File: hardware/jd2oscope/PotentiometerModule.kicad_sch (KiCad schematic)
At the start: 1 part

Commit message: feat: lot of progress
added decoupling caps, implemented a lot more of the comm. protocol stuffs, updated BNC connector to updated version, added more notes for GPIO pin I/O for future code implementation, lot of other stuff too (frankly can't remember all of it lol); I commit here b/c want to back up progress b/4 I go get smth to eat ;)
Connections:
- net reg.3.3V: now reaches VR1.1
- net POT_WIPER: now reaches VR1.2
- net GND: now reaches VR1.3
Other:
- note added: "Example of implementing POT_WIPER's GPIO pin to read % in code:"
- note added: "Key: input = 3.3V (b/c this is for logicV & we can't do 5V to GPIO pins (5V breaks them)); supplied from the 3.3V reg. on the MCU output = GND wiper = represents how much the pot. is currently rotated (i.e. the ratio between I & O)"

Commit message: feat: finished schematics
I think! Subject to change tho! for now though at least, I think they look clean asf hah~
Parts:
- renumbered VR1 to VR2
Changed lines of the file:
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@@
 		(dnp no)
 		(fields_autoplaced yes)
-		(property "Reference" "VR1"
+		(property "Reference" "VR2"
 			(at 142.24 86.36 0)
 			(effects
@@
 		)
 		(instances
-			(project ""
-				(path "/eb18a3da-9fbf-4329-a814-1afab785c817/dff6ec06-2d4b-4768-9220-df3b02ec1774"
+			(project "jd2oscope"
+				(path "/eb18a3da-9fbf-4329-a814-1afab785c817/415ed027-7cd2-4459-ae99-e85a85aec1e2/0b10fb84-a9af-450b-b4ba-7677bde7a4aa"
+					(reference "VR3")
+					(unit 1)
+				)
+				(path "/eb18a3da-9fbf-4329-a814-1afab785c817/415ed027-7cd2-4459-ae99-e85a85aec1e2/34809825-0d94-4631-a2d1-f31cc7a3b6ba"
+					(reference "VR2")
+					(unit 1)
+				)
+				(path "/eb18a3da-9fbf-4329-a814-1afab785c817/415ed027-7cd2-4459-ae99-e85a85aec1e2/4f25ad0e-659b-4d0d-998d-272f66fe29fb/a129be14-5636-4b2f-ac25-6f79cead8126"
+					(reference "VR4")
+					(unit 1)
+				)
+				(path "/eb18a3da-9fbf-4329-a814-1afab785c817/415ed027-7cd2-4459-ae99-e85a85aec1e2/4f25ad0e-659b-4d0d-998d-272f66fe29fb/d0d3e5b7-5e05-4d56-af40-3a75a71576b8"
 					(reference "VR1")
 					(unit 1)
 				)
+				(path "/eb18a3da-9fbf-4329-a814-1afab785c817/415ed027-7cd2-4459-ae99-e85a85aec1e2/9cf642e2-7276-4116-93a5-7485645ddebf/a129be14-5636-4b2f-ac25-6f79cead8126"
+					(reference "VR6")
+					(unit 1)
+				)
+				(path "/eb18a3da-9fbf-4329-a814-1afab785c817/415ed027-7cd2-4459-ae99-e85a85aec1e2/9cf642e2-7276-4116-93a5-7485645ddebf/d0d3e5b7-5e05-4d56-af40-3a75a71576b8"
+					(reference "VR5")
+					(unit 1)
+				)

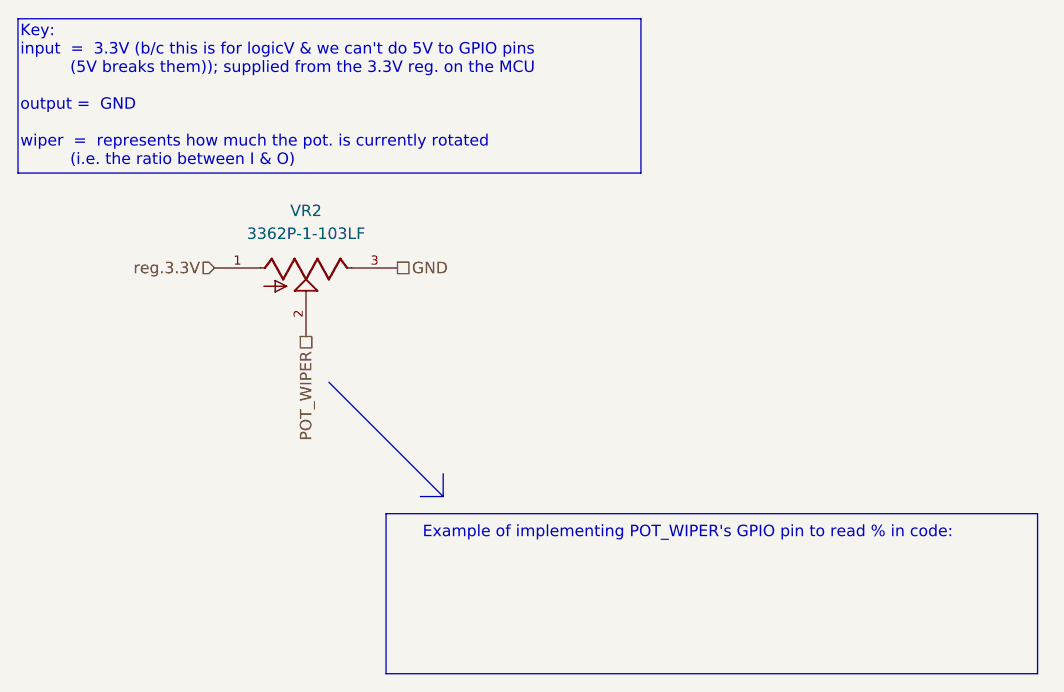
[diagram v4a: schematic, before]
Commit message: fix: added NCs
forgot to add NCs to Wroom32 dev board; they are now added!
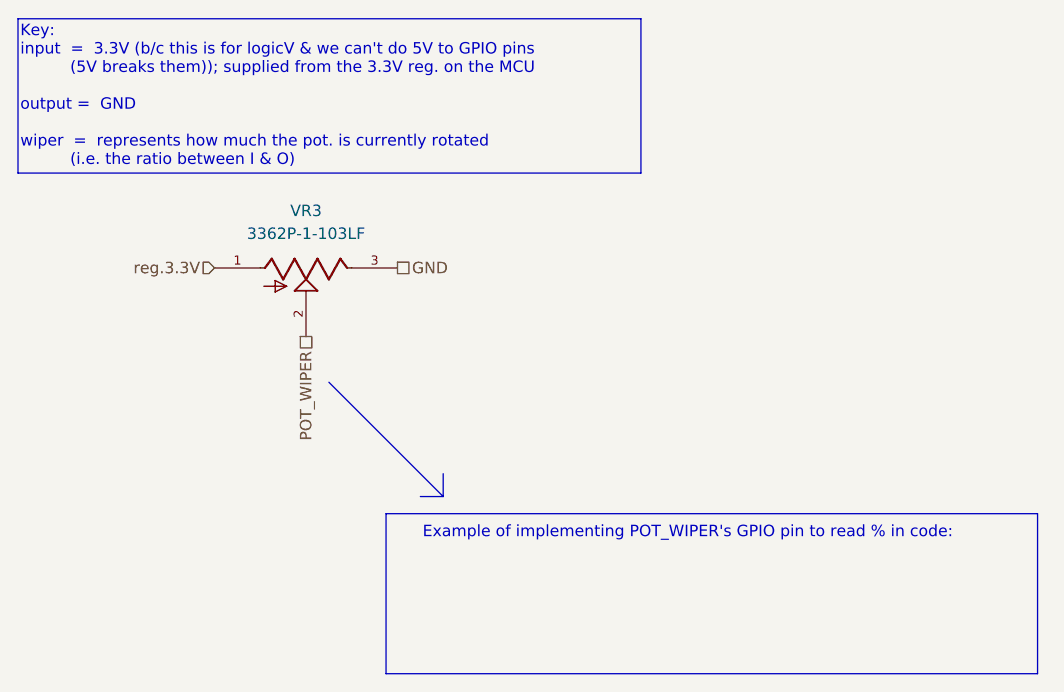
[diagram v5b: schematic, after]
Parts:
- renumbered VR2 to VR3
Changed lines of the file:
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@@
 		(dnp no)
 		(fields_autoplaced yes)
-		(property "Reference" "VR2"
+		(property "Reference" "VR3"
 			(at 142.24 86.36 0)
 			(effects

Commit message: fix: ERC funtimes
fixed a bunch of dependencies with ERC checks for the schematic; shouuuuld be easier/actually possible to open on other devices now?? (added a buncha schematics & footprints to the local files & whatnot)
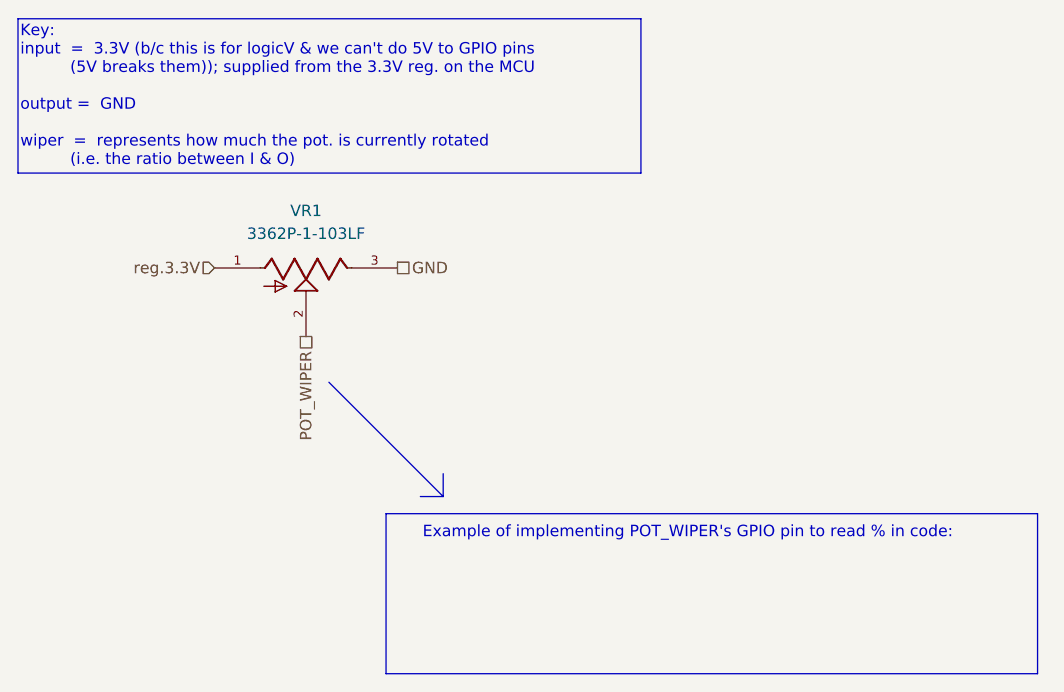
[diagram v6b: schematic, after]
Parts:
- removed VR3: 3362P-1-103LF, 3362P-1-103LF:TRIM_3362P-1-103LF, symbol pot:3362P-1-103LF
- added VR1: 3362P-1-103LF, 3362P-1-103LF:TRIM_3362P-1-103LF, symbol 3362P-1-103LF:3362P-1-103LF
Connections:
- net GND: now also VR1.3
- net POT_WIPER: now also VR1.2
- net reg.3.3V: now also VR1.1
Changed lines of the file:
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@@
 	)
 	(symbol
-		(lib_id "pot:3362P-1-103LF")
+		(lib_id "3362P-1-103LF:3362P-1-103LF")
 		(at 142.24 92.71 0)
 		(unit 1)
@@
 		(dnp no)
 		(fields_autoplaced yes)
-		(property "Reference" "VR3"
+		(property "Reference" "VR1"
 			(at 142.24 86.36 0)
 			(effects
@@
 			)
 		)
-		(property "Sim.Device" ""
-			(at 142.24 92.71 0)
-			(effects
-				(font
-					(size 1.27 1.27)
-				)
-				(hide yes)
-			)
-		)
-		(property "Sim.Params" ""
-			(at 142.24 92.71 0)
-			(effects
-				(font
-					(size 1.27 1.27)
-				)
-				(hide yes)
-			)
-		)
-		(property "Sim.Pins" ""
-			(at 142.24 92.71 0)
-			(effects
-				(font
-					(size 1.27 1.27)
-				)
-				(hide yes)
-			)
-		)
-		(property "Sim.Type" ""
-			(at 142.24 92.71 0)
-			(effects
-				(font
-					(size 1.27 1.27)
-				)
-				(hide yes)
-			)
-		)
-		(property "Comment" ""
-			(at 142.24 92.71 0)
-			(effects
-				(font
-					(size 1.27 1.27)
-				)
-				(hide yes)
-			)
-		)
-		(property "EU_RoHS_Compliance" ""
-			(at 142.24 92.71 0)
-			(effects
-				(font
-					(size 1.27 1.27)
-				)
-				(hide yes)
-			)
-		)
-		(property "Number_of_Positions" ""
-			(at 142.24 92.71 0)
-			(effects
-				(font
-					(size 1.27 1.27)
-				)
-				(hide yes)
-			)
+		(pin "2"
 		)
 		(pin "1"
@@
 		(pin "3"
 		)
-		(pin "2"
-		)
 		(instances
 			(project "jd2oscope"
 				(path "/eb18a3da-9fbf-4329-a814-1afab785c817/415ed027-7cd2-4459-ae99-e85a85aec1e2/0b10fb84-a9af-450b-b4ba-7677bde7a4aa"
+					(reference "VR4")
+					(unit 1)
+				)
+				(path "/eb18a3da-9fbf-4329-a814-1afab785c817/415ed027-7cd2-4459-ae99-e85a85aec1e2/34809825-0d94-4631-a2d1-f31cc7a3b6ba"
 					(reference "VR3")
 					(unit 1)
 				)
-				(path "/eb18a3da-9fbf-4329-a814-1afab785c817/415ed027-7cd2-4459-ae99-e85a85aec1e2/34809825-0d94-4631-a2d1-f31cc7a3b6ba"
+				(path "/eb18a3da-9fbf-4329-a814-1afab785c817/415ed027-7cd2-4459-ae99-e85a85aec1e2/4f25ad0e-659b-4d0d-998d-272f66fe29fb/a129be14-5636-4b2f-ac25-6f79cead8126"
 					(reference "VR2")
 					(unit 1)
 				)
-				(path "/eb18a3da-9fbf-4329-a814-1afab785c817/415ed027-7cd2-4459-ae99-e85a85aec1e2/4f25ad0e-659b-4d0d-998d-272f66fe29fb/a129be14-5636-4b2f-ac25-6f79cead8126"
-					(reference "VR4")
-					(unit 1)
-				)

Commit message: fix: footprint/symbol fixes for ILI9341_Touch
blegh
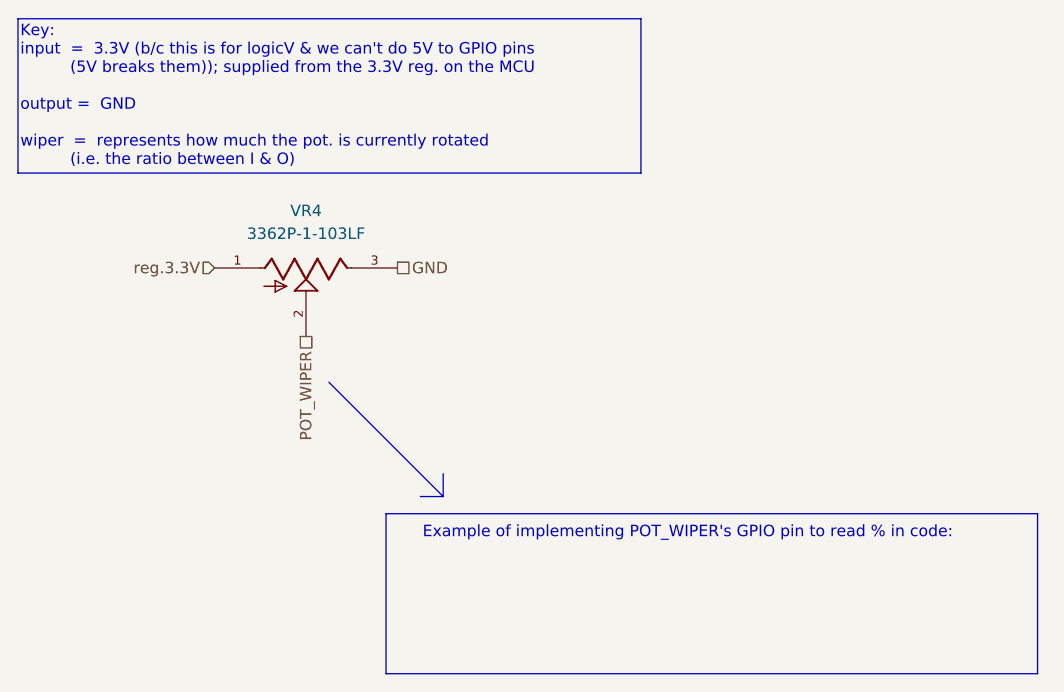
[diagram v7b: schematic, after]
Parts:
- renumbered VR1 to VR4
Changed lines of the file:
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@@
 		(dnp no)
 		(fields_autoplaced yes)
-		(property "Reference" "VR1"
+		(property "Reference" "VR4"
 			(at 142.24 86.36 0)
 			(effects

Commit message: feat/fix: no more errors for PCB import too!
Now both the ERC, and the schematic import (and my OCD) are completely satisfied, and we can dev the actual PCB; let's go!! :D
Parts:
- VR4: footprint 3362P-1-103LF:TRIM_3362P-1-103LF -> jd2Oscope_Footprints:TRIM_3362P-1-103LF
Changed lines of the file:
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@@
 			)
 		)
-		(property "Footprint" "3362P-1-103LF:TRIM_3362P-1-103LF"
+		(property "Footprint" "jd2Oscope_Footprints:TRIM_3362P-1-103LF"
 			(at 142.24 92.71 0)
 			(effects
